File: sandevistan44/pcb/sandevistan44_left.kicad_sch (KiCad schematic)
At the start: 48 parts, among them J1 TRRS, SW1 SW_PUSH, SW10 SW_PUSH, SW11 SW_PUSH, SW12 SW_PUSH, SW13 SW_PUSH, SW14 SW_PUSH, SW15 SW_PUSH, SW16 SW_PUSH, SW17 SW_PUSH, SW18 SW_PUSH, SW19 SW_PUSH, SW2 SW_PUSH, SW20 SW_PUSH, SW21 SW_PUSH, SW22 SW_PUSH, SW3 SW_PUSH, SW4 SW_PUSH, SW5 SW_PUSH, SW6 SW_PUSH, SW7 SW_PUSH, SW8 SW_PUSH, SW9 SW_PUSH, U1 ProMicro

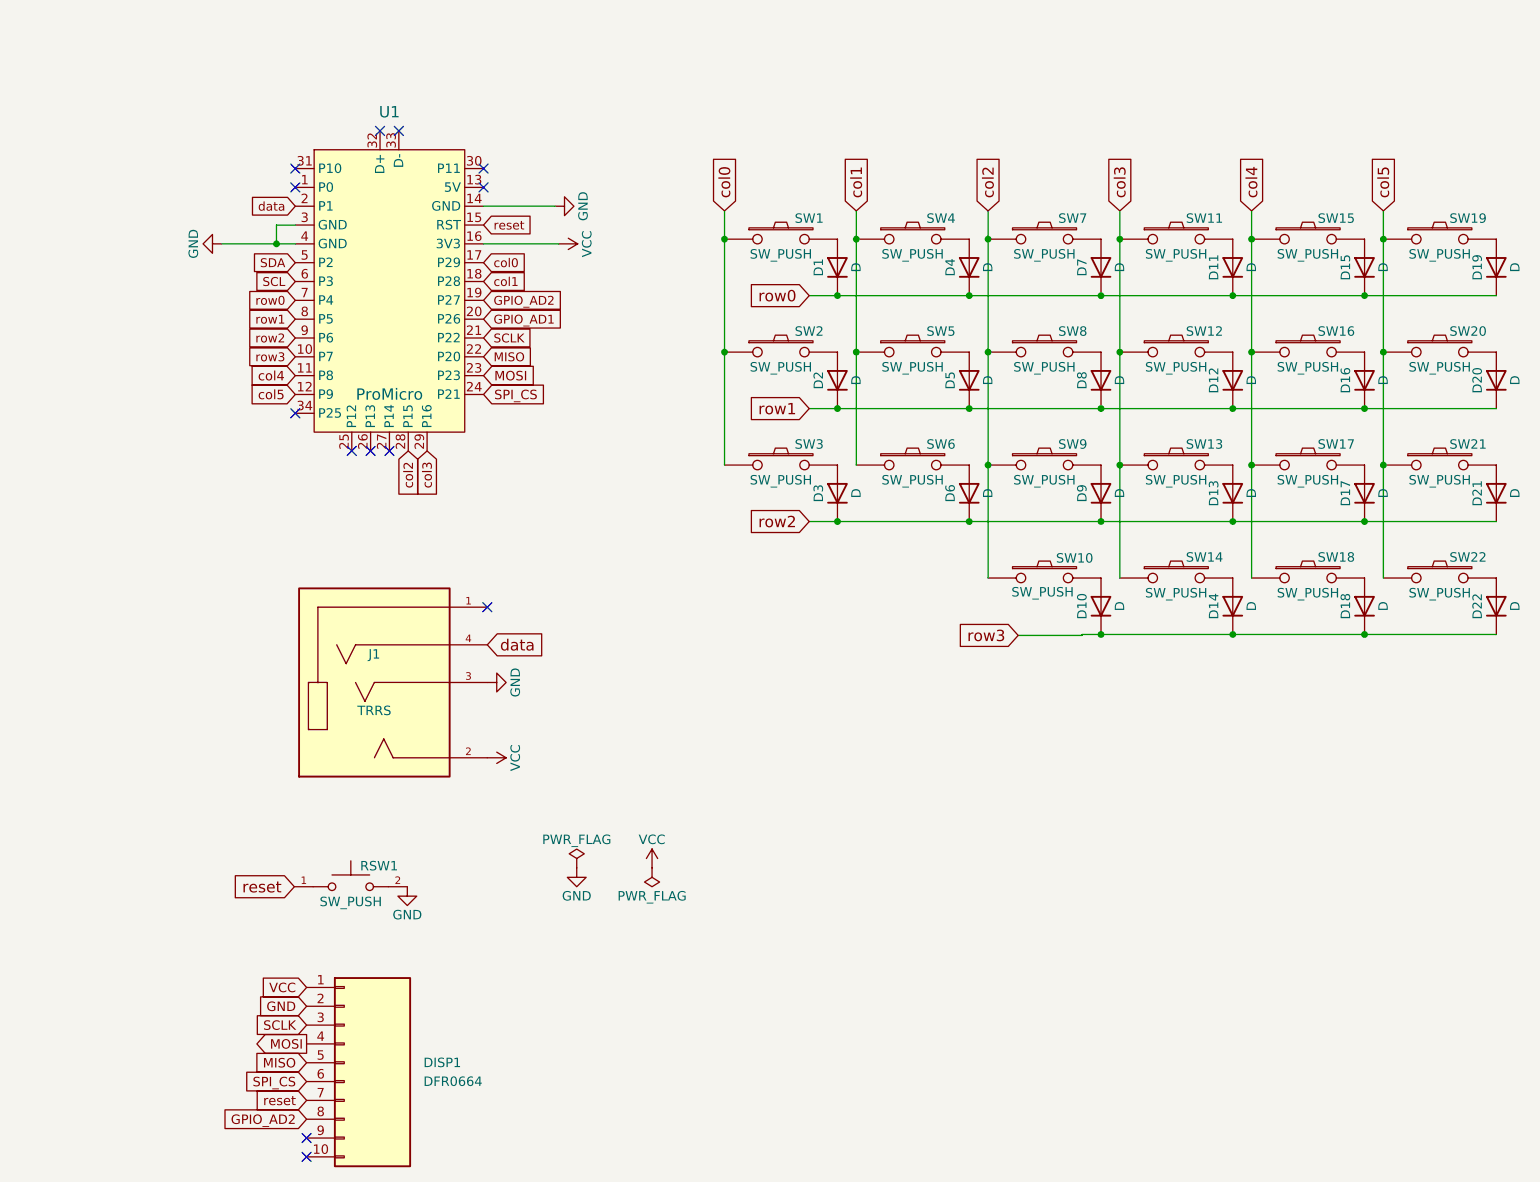
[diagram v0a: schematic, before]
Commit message: Start rev0.2 build
- pi pico replaces pro micro style mcu
- mcu now on underside
- rewire for simplicity
- update switch footprints to allow choc, mx, gateron lp
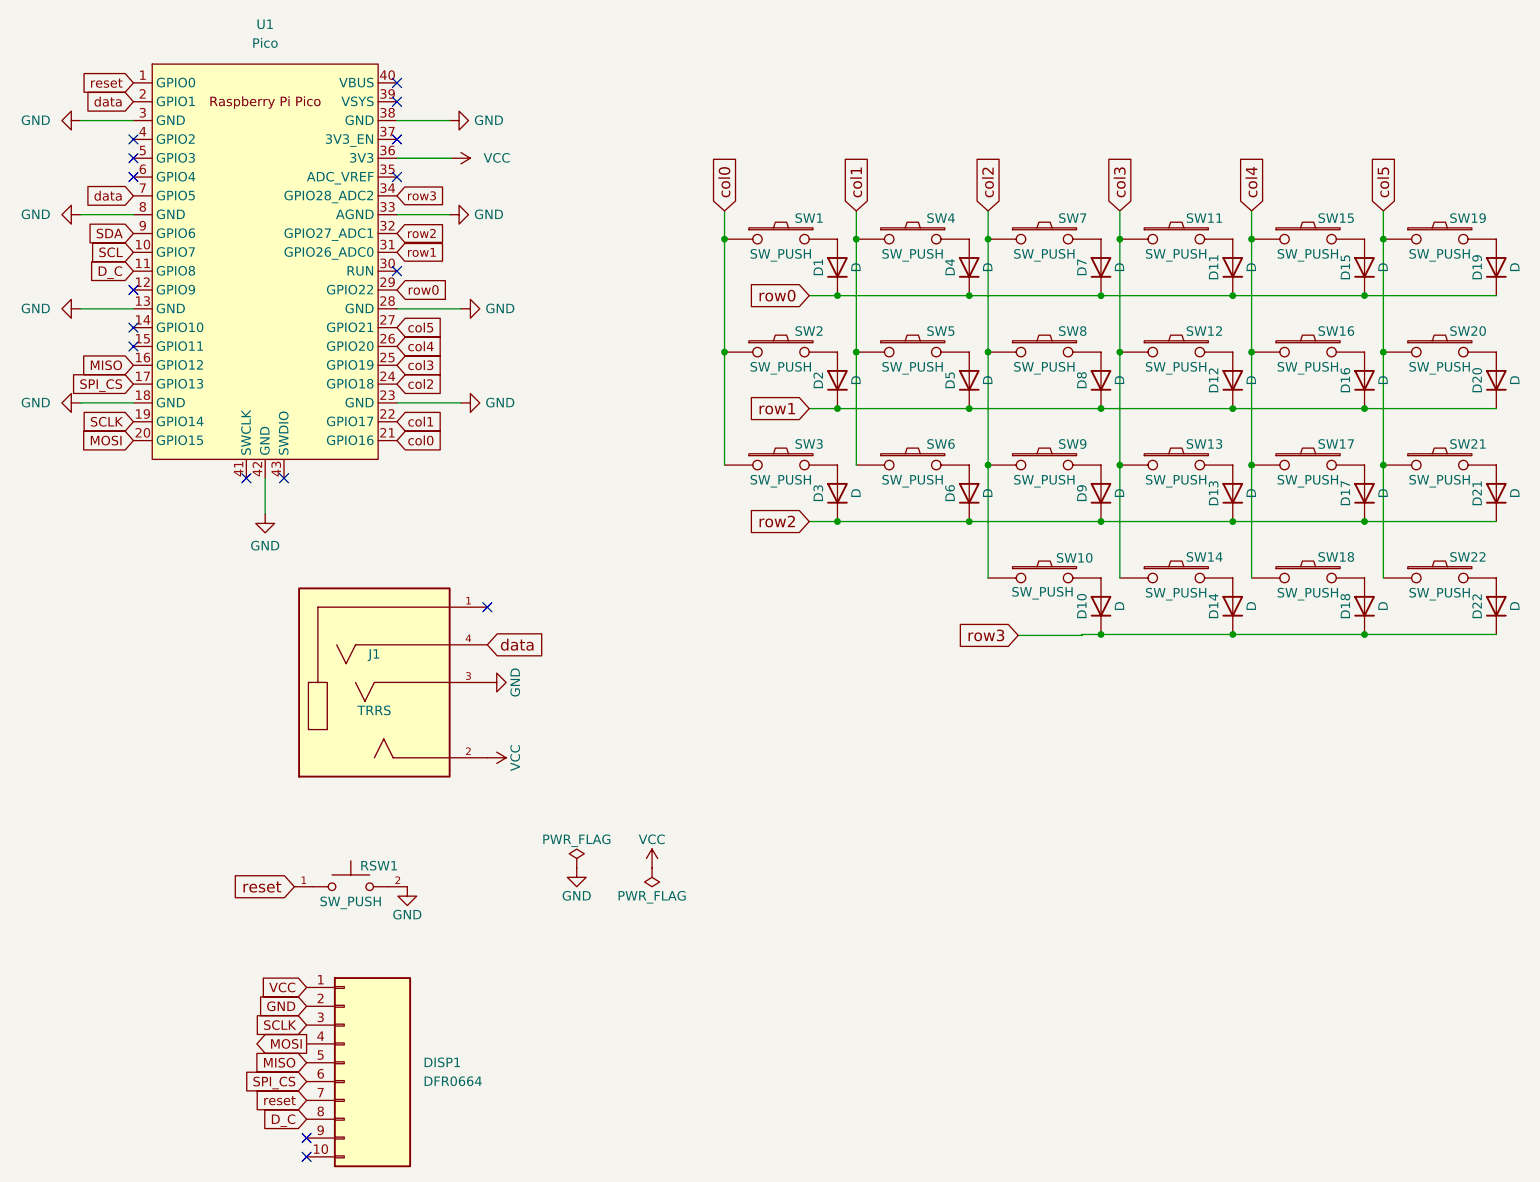
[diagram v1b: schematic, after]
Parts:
- removed U1: ProMicro, marbastlib-xp-promicroish:Helios_AC, symbol marbastlib-promicroish:Helios
- added U1: Pico, Library:RPi_Pico_SMD_TH_no_through_holes, symbol MCU_RaspberryPi_and_Boards:Pico
- SW1, SW10, SW11, SW12, SW13, SW14, SW15, SW16, SW17, SW18, SW19, SW2, SW20, SW21, SW3, SW4, SW5, SW6, SW7, SW8, SW9: footprint Library:SW_Hotswap_Kailh_Choc_V2_1.00u -> Library:Universal Switch Footprint (1u)
- SW22: footprint Library:SW_Hotswap_Kailh_Choc_V2_1.25u -> Library:Universal Switch Footprint (1.5u)
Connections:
- net GND: now also U1.13 (GND), U1.18 (GND), U1.23 (GND), U1.28 (GND), U1.3 (GND), U1.33 (AGND), U1.38 (GND), U1.42 (GND), U1.8 (GND)
- net MISO: now also U1.16 (GPIO12)
- net MOSI: now also U1.20 (GPIO15)
- net SCL: now also U1.10 (GPIO7)
- net SCLK: now also U1.19 (GPIO14)
- net SDA: now also U1.9 (GPIO6)
- net SPI_CS: now also U1.17 (GPIO13)
- net VCC: now also U1.36 (3V3)
- net col0: now also U1.21 (GPIO16)
- net col1: now also U1.22 (GPIO17)
- net col2: now also U1.24 (GPIO18)
- net col3: now also U1.25 (GPIO19)
- net col4: now also U1.26 (GPIO20)
- net col5: now also U1.27 (GPIO21)
- net data: now also U1.2 (GPIO1), U1.7 (GPIO5)
- net reset: now also U1.1 (GPIO0)
- net row0: now also U1.29 (GPIO22)
- net row1: now also U1.31 (GPIO26_ADC0)
- net row2: now also U1.32 (GPIO27_ADC1)
- net row3: now also U1.34 (GPIO28_ADC2)
- net GPIO_AD2 renamed D_C
- net D_C: now also U1.11 (GPIO8)
- no-connect marks 13 -> 16

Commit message: Finish first iteration of 0.2 configuration
- Add encoders on each side and add body extension
- Modify trackball module cutout to allow for up to 55mm trackball
- Rewire again to fit new layout
- Fix/cleanup footprints
- Rework standoff holes to fit with new switch footprints
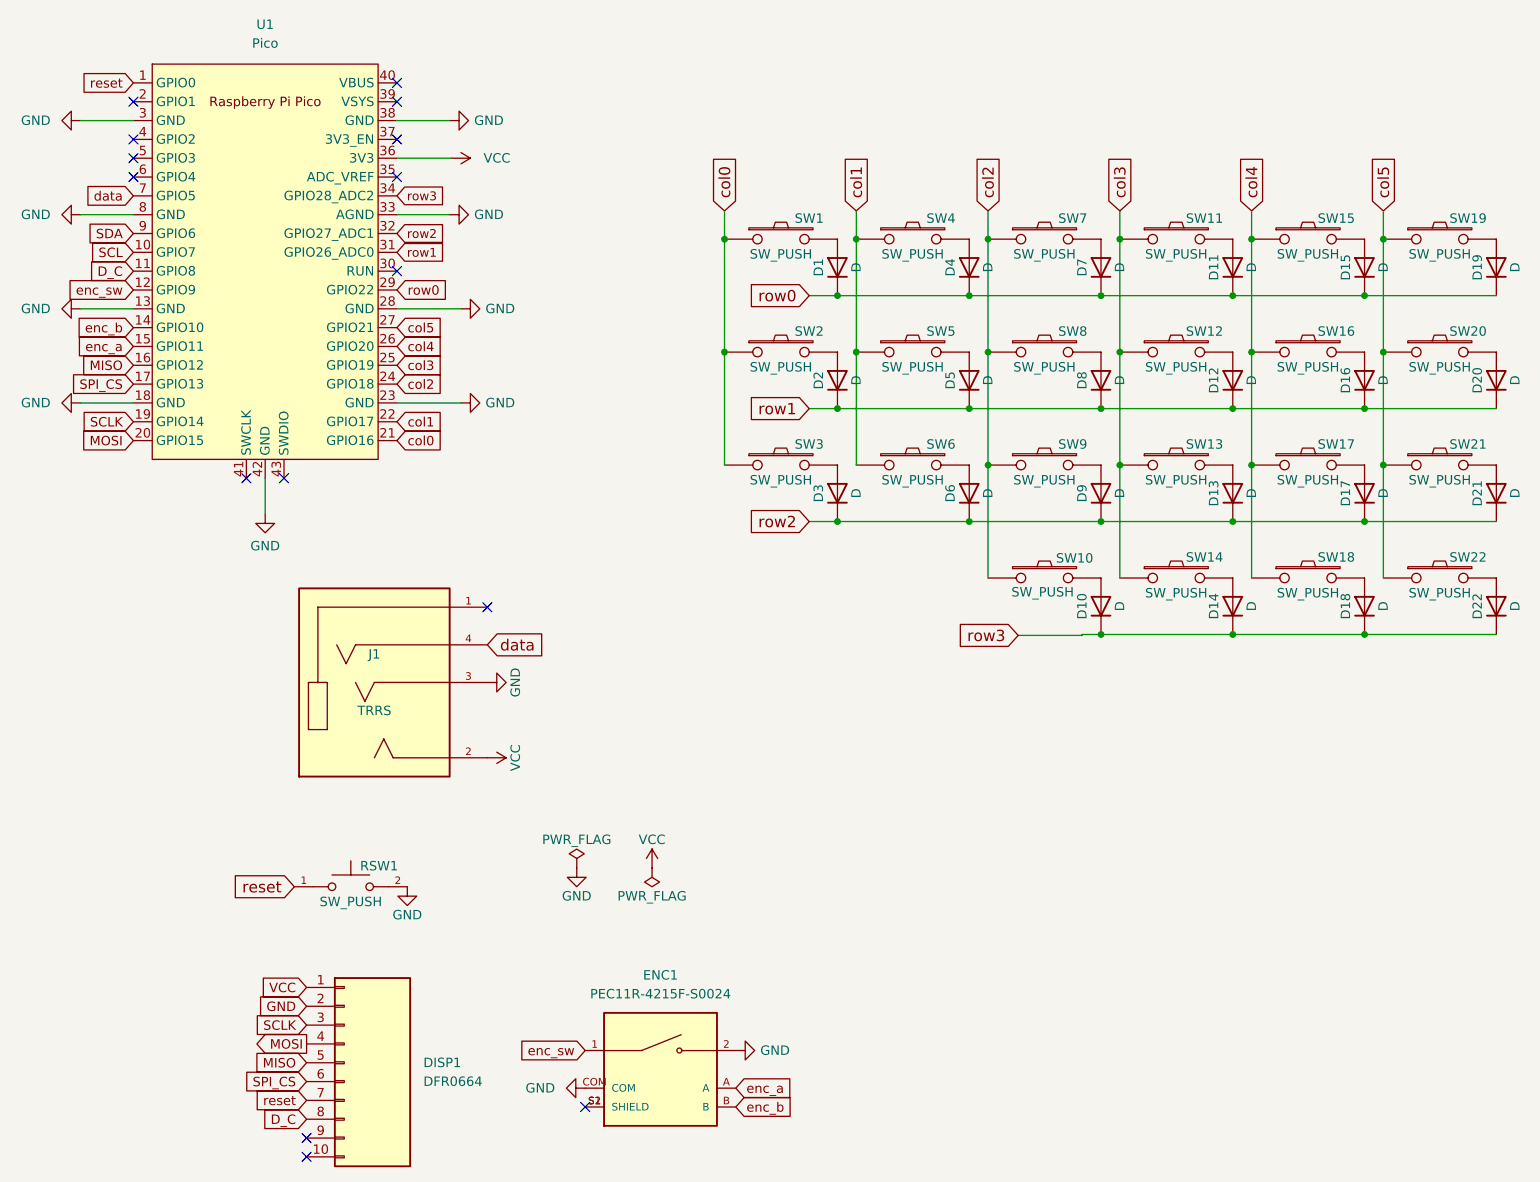
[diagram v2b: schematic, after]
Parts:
- added ENC1: PEC11R-4215F-S0024, PEC11R-4215F-S0024:XDCR_PEC11R-4215F-S0024, symbol PEC11R-4215F-S0024:PEC11R-4215F-S0024
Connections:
- net GND: now also ENC1.2, ENC1.COM
- net data: no longer U1.2 (GPIO1)
- net enc_sw: now reaches U1.12 (GPIO9)
- net enc_sw: now also ENC1.1
- net enc_b: now reaches U1.14 (GPIO10)
- net enc_b: now also ENC1.B
- net enc_a: now reaches U1.15 (GPIO11)
- net enc_a: now also ENC1.A
- new net: ENC1.S1 (SHIELD), ENC1.S2 (SHIELD)
- no-connect marks 16 -> 15

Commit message: Finalize left and right board setups
- Rework thumb cluster layout left and right
- Rework board shape on left and right
- Remove encoder from left side
- Rework wiring for better cleanliness/safety
- Reposition some standoff holes
- Move mouse button FFC connector
- Repin MCUs left and right for better routing
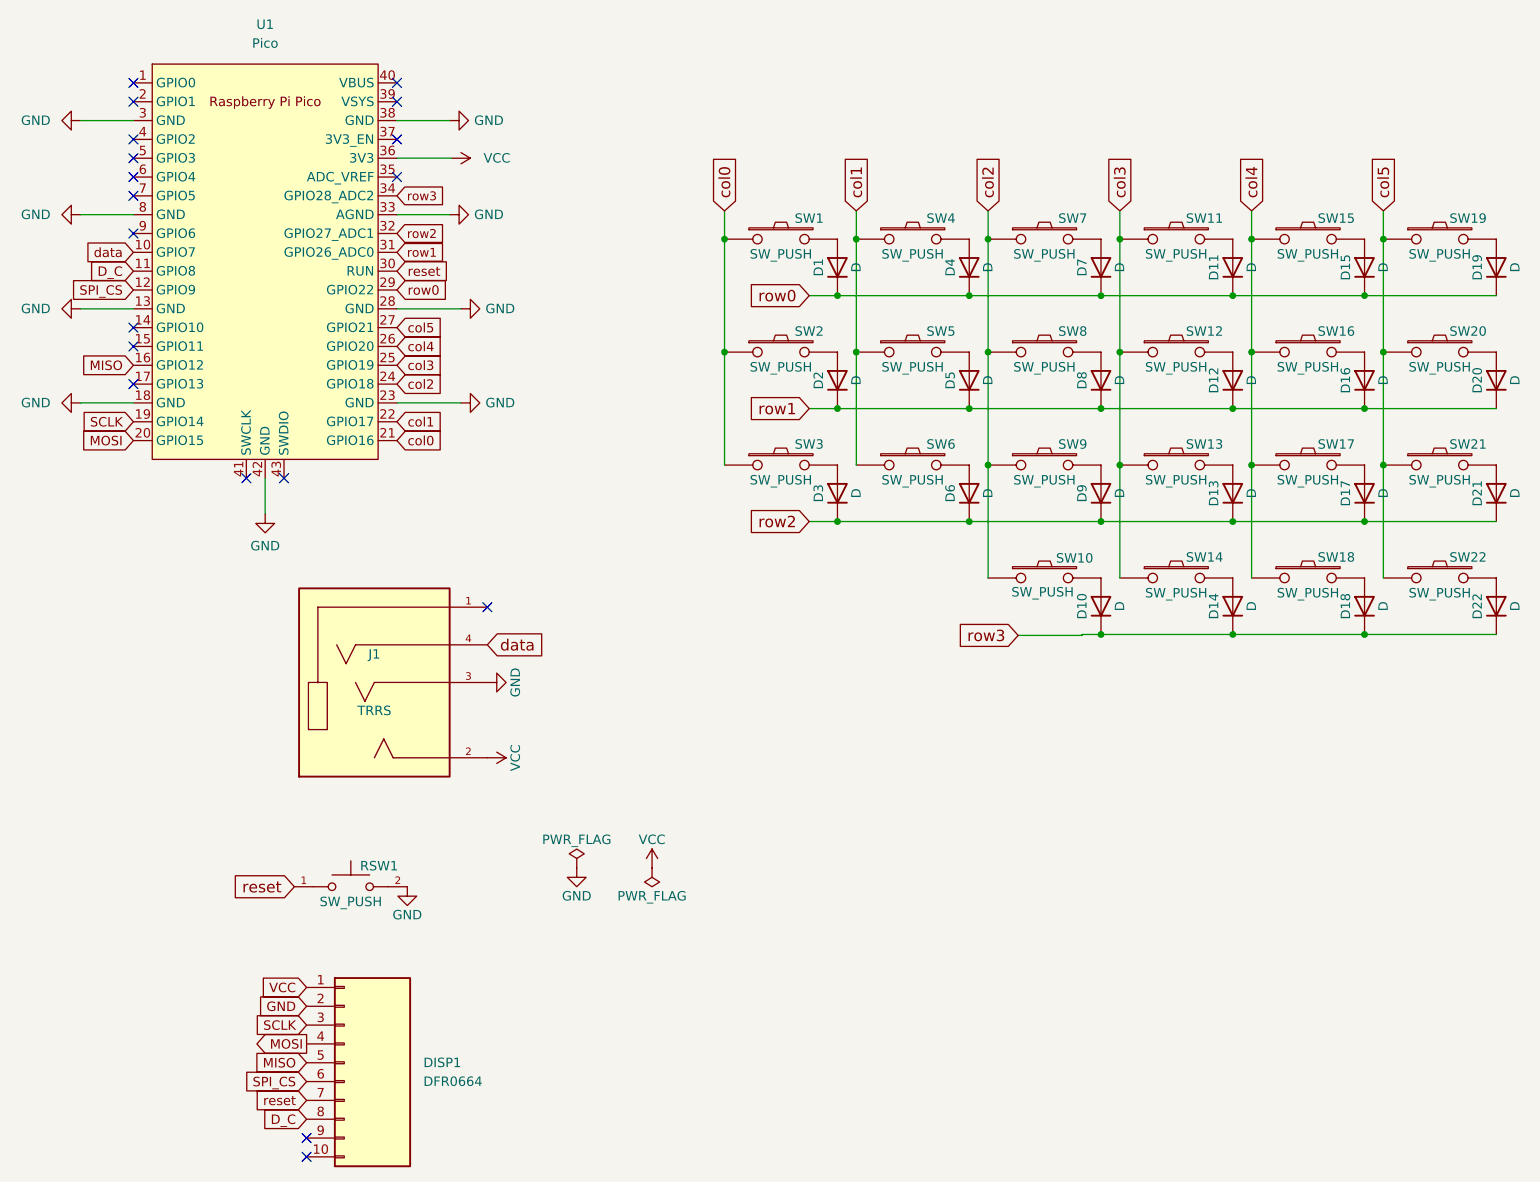
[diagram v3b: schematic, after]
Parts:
- removed ENC1: PEC11R-4215F-S0024, PEC11R-4215F-S0024:XDCR_PEC11R-4215F-S0024, symbol PEC11R-4215F-S0024:PEC11R-4215F-S0024
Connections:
- net SCL is gone; now on net data: U1.10 (GPIO7)
- net enc_sw is gone; now on net SPI_CS: U1.12 (GPIO9)
- net SPI_CS: no longer U1.17 (GPIO13)
- net data: no longer U1.7 (GPIO5)
- net reset: now also U1.30 (RUN); no longer U1.1 (GPIO0)
- net SDA: no longer names the net of U1.9 (GPIO6)
- net enc_a: no longer names the net of U1.15 (GPIO11)
- net enc_b: no longer names the net of U1.14 (GPIO10)
- no-connect marks 15 -> 19
